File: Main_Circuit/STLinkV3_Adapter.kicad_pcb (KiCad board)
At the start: 2 copper layers, 32 x 48.6 mm, 10 parts, among them J1 Conn_01x03_Male, J2 Conn_01x05_Male, J3 Conn_01x04_Male, J4 Conn_01x05_Male, J5 Conn_01x04_Male, J6 Conn_01x06_Male, J7 Conn_01x06_Male, U1 STLINK-V3MODS

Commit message: Design PCB completed
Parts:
- added G***: LOGO, STLINK-V3MODS:GITHUB LOGO, B.Cu at (93.7, 63.1)
- moved J3 12.6 mm to (72.0, 94.8)
- moved J2 10.9 mm to (72.0, 78.8), turned to 180 degrees
- moved J1 5.18 mm to (99.8, 95.2), turned to 0 degrees
- moved J5 3.60 mm to (72.0, 90.6), turned to 180 degrees
- moved R1 2.16 mm to (97.7, 81.7), turned to 90 degrees
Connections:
- J1 pad 1: /GND -> GNDREF
- J2 pad 1: /GND -> GNDREF
- J3 pad 1: /GND -> GNDREF
- J4 pad 1: /GND -> GNDREF
- J5 pad 1: /GND -> GNDREF
- J6 pad 3: /GND -> GNDREF
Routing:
- net /5V: track 0.00 -> 83.5 mm, vias 0 -> 1
- net /T_NRST: track 0.00 -> 51.1 mm, vias 0 -> 2
- net /SPI_NSS: track 0.00 -> 44.8 mm, vias 0 -> 1
- net /T_GND: track 2.25 -> 45.4 mm, vias 0 -> 2
- net /T_SWDIO: track 0.00 -> 42.7 mm, vias 0 -> 2
- net /T_VCC: track 0.00 -> 36.7 mm, vias 0 -> 1
- net /T_SWCLK: track 0.00 -> 36.4 mm, vias 0 -> 2
- net /T_SWO: track 0.00 -> 34.1 mm, vias 0 -> 1
- net /SPI_CLK: track 0.00 -> 29.1 mm, vias 0 -> 1
- net /I2C_SCL: track 0.00 -> 27.7 mm
- net /UART_Tx: track 0.00 -> 18.1 mm, vias 0 -> 2
- net /VCP_Tx: track 7.04 -> 20.4 mm
- net /VCP_Rx: track 6.85 -> 19.5 mm
- net /I2C_SDA: track 0.00 -> 12.3 mm
- net /CAN_Tx: track 0.00 -> 11.5 mm
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- added copper zone on B.Cu, net GNDREF
- added copper zone on F.Cu, net GNDREF
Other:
- outline, holes or cut-outs redrawn
- board text added: "5V"
- board text added: "@tw1chao"
- board text added: "CAN"
- board text added: "CLK"
- board text added: "CTS"
- board text added: "DIO"
- board text added: "GND"
- board text added: "GPIO"
- board text added: "I2C"
- board text added: "IO0"
- board text added: "IO1"
- board text added: "IO2"
- board text added: "IO3"
- board text added: "NSS"
- board text added: "RST"
- board text added: "RTS"
- board text added: "Rx"
- board text added: "SCL"
- board text added: "SDA"
- board text added: "SDI"
- board text added: "SDO"
- board text added: "SPI"
- board text added: "STLINK"
- board text added: "SWO"
- board text added: "Tx"
- board text added: "USART"
- board text added: "VCC"
- board text added: "VCP"
- board text added: "yingchao.tw@gmail.com"

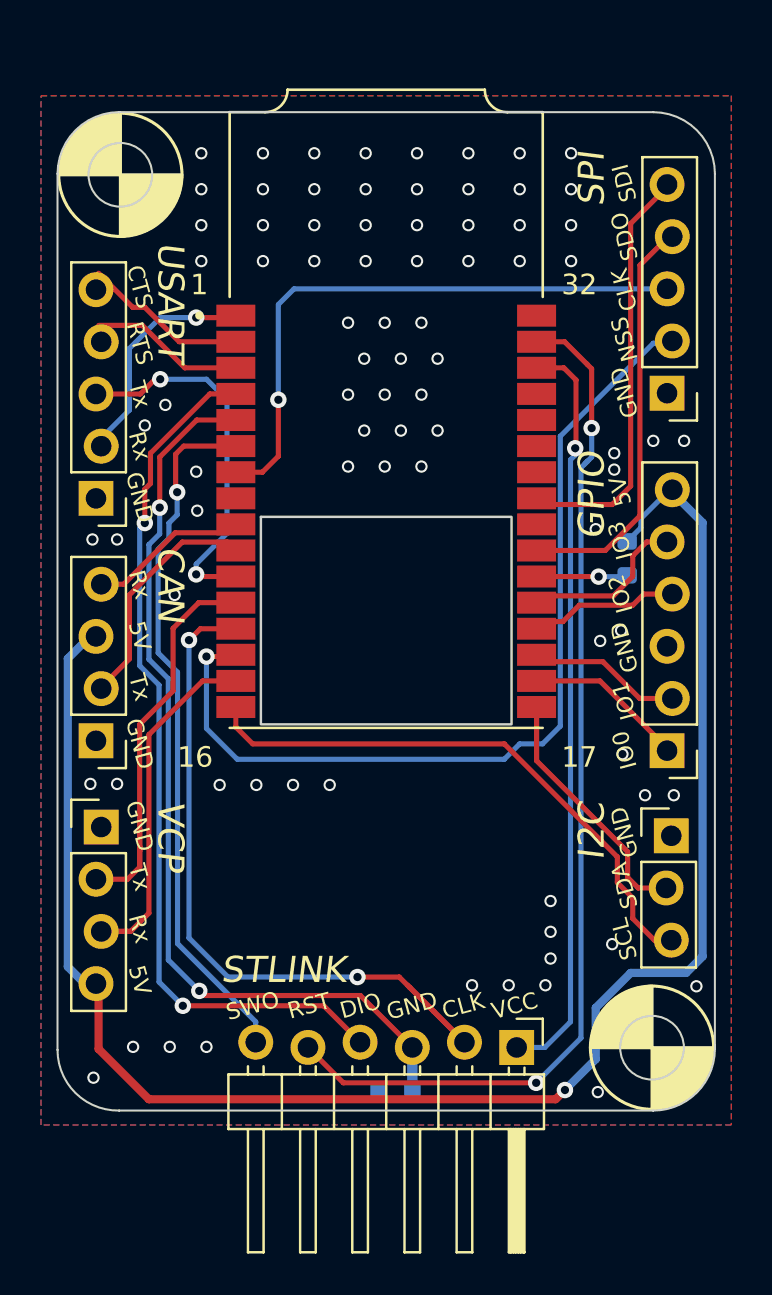
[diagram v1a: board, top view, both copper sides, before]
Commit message: modifly pin header connector dis
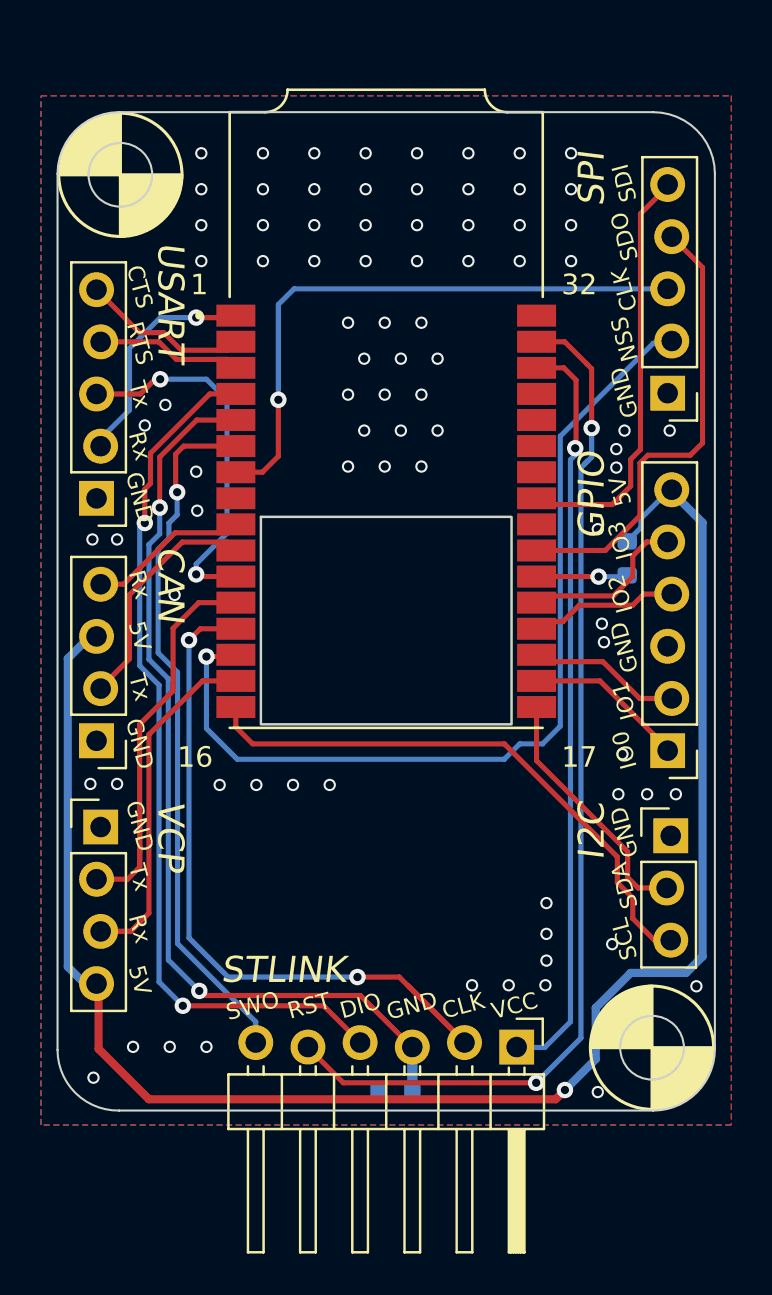
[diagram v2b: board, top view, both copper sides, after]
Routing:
- net /SPI_MISO: track 20.0 -> 22.5 mm
- net GNDREF: vias 83 -> 84
